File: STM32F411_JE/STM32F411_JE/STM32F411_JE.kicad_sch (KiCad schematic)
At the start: 1 part, among them U1 STM32F411CEU6

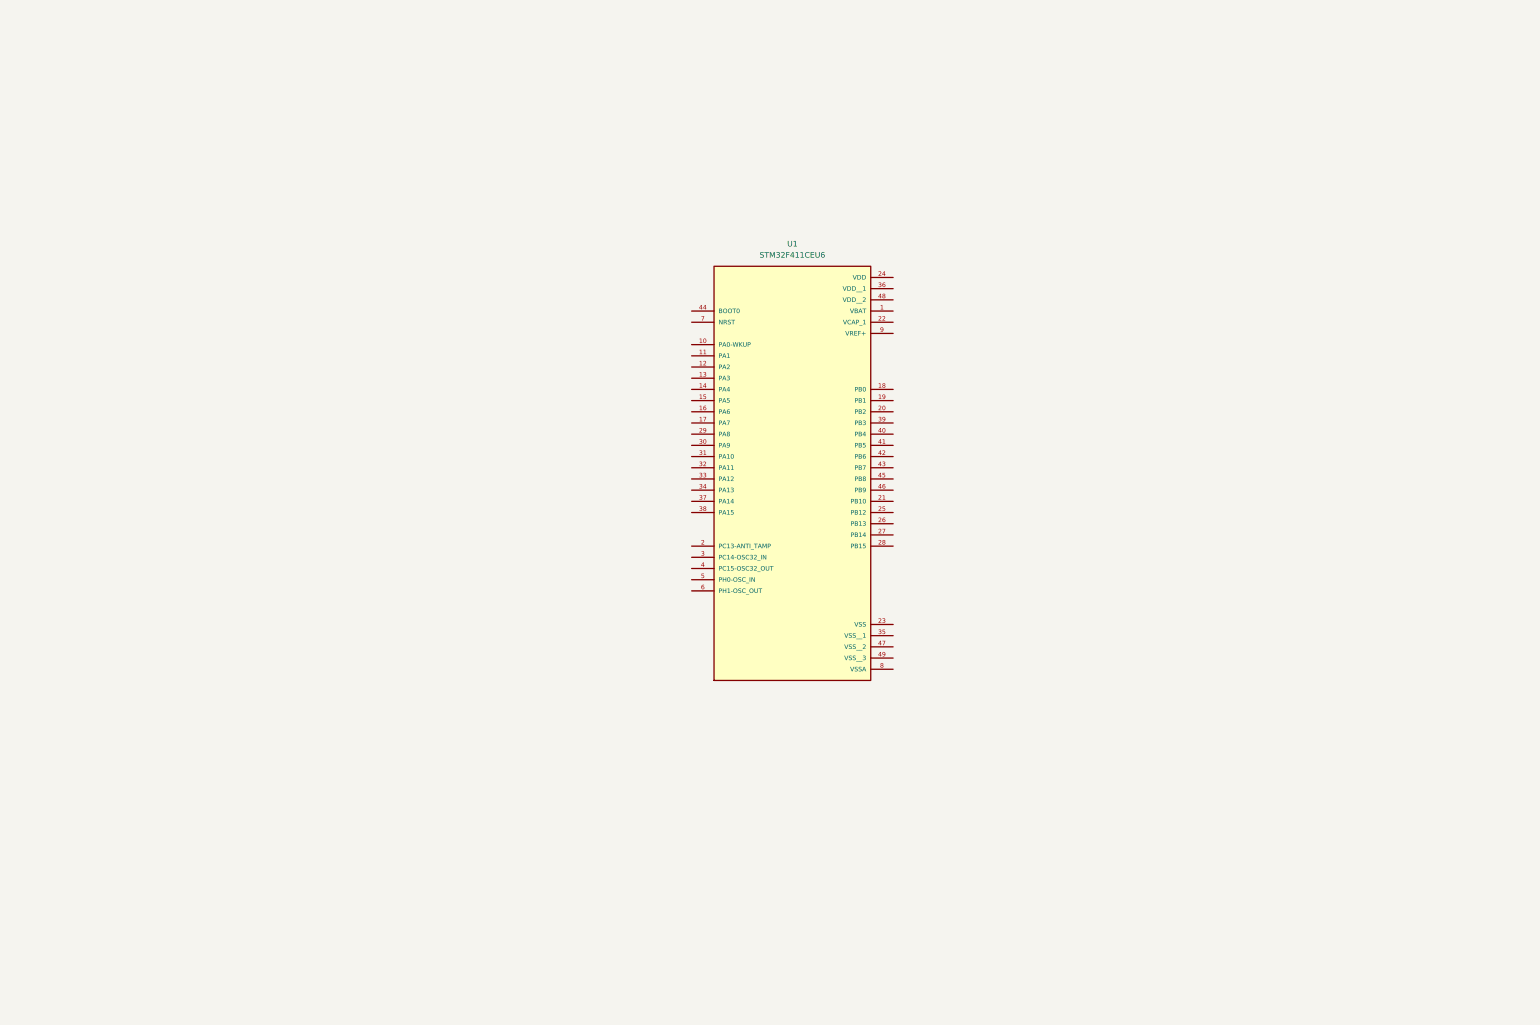
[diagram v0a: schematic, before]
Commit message: Se agrega el circuito de boot, de alimentación, de reset, y alimentación del rtc
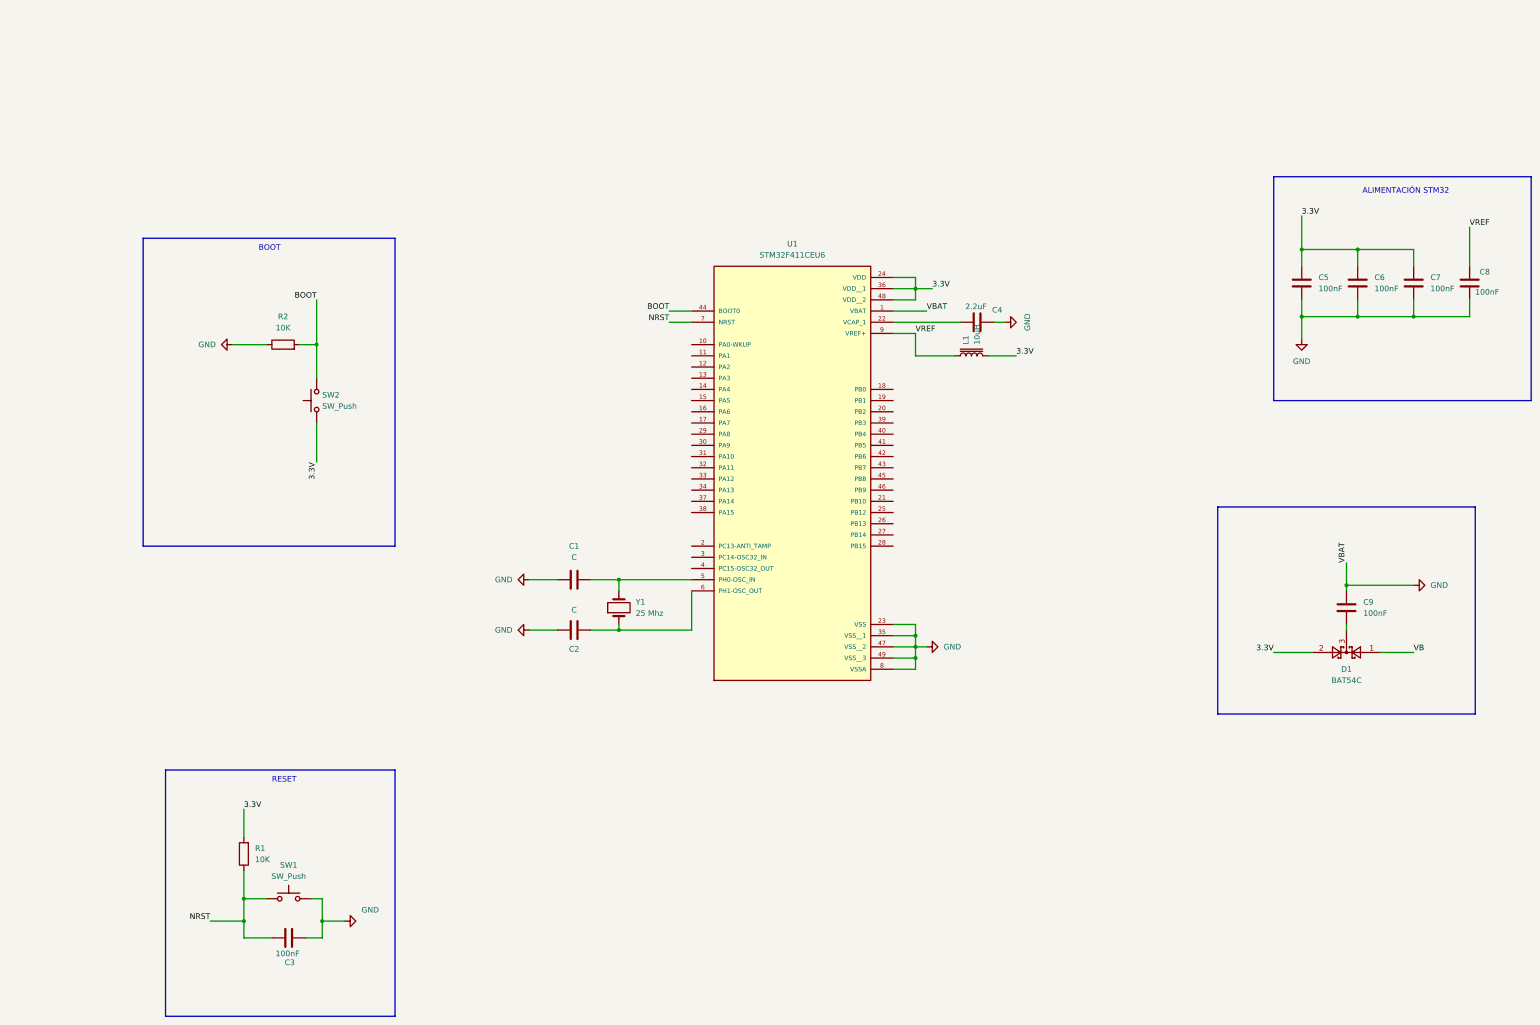
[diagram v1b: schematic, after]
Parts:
- added C1, C2: C, symbol Device:C
- added C3, C5, C6, C7, C8, C9: 100nF, Capacitor_SMD:C_0603_1608Metric_Pad1.08x0.95mm_HandSolder, symbol Device:C
- added C4: 2.2uF, Capacitor_SMD:C_0603_1608Metric_Pad1.08x0.95mm_HandSolder, symbol Device:C
- added D1: BAT54C, Package_TO_SOT_SMD:SOT-23, symbol Diode:BAT54C
- added L1: 10uH, Inductor_SMD:L_0603_1608Metric, symbol Device:L_Iron
- added R1, R2: 10K, Resistor_SMD:R_0603_1608Metric_Pad0.98x0.95mm_HandSolder, symbol Device:R
- added SW1, SW2: SW_Push, Button_Switch_SMD:SW_SPST_CK_RS282G05A3, symbol Switch:SW_Push
- added Y1: 25 Mhz, symbol Device:Crystal
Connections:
- net GND: now reaches U1.1 (VBAT)
- net GND: now also U1.23 (VSS), U1.35 (VSS__1), U1.47 (VSS__2), U1.49 (VSS__3), U1.8 (VSSA), C1.1, C2.1, C3.2, C4.1, C5.2, C6.2, C7.2, C8.2, C9.1, R2.1, SW1.2
- net at U1.22 (VCAP_1): now also C4.2
- net 3.3V: now reaches U1.24 (VDD)
- net 3.3V: now also U1.36 (VDD__1), U1.48 (VDD__2), C5.1, C6.1, C7.1, D1.2, L1.2, R1.2, SW2.1
- net BOOT: now reaches U1.44 (BOOT0)
- net BOOT: now also R2.2, SW2.2
- net at U1.5 (PH0-OSC_IN): now also C1.2, Y1.2
- net at U1.6 (PH1-OSC_OUT): now also C2.2, Y1.1
- net NRST: now reaches U1.7 (NRST)
- net NRST: now also C3.1, R1.1, SW1.1
- net VREF: now reaches U1.9 (VREF+)
- net VREF: now also C8.1, L1.1
- new net: C9.2, D1.3
- new net VB: D1.1
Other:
- note added: "ALIMENTACIÓN STM32"
- note added: "BOOT"
- note added: "RESET"

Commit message: Se termina el diseño esquematico de el STM32F411_JE
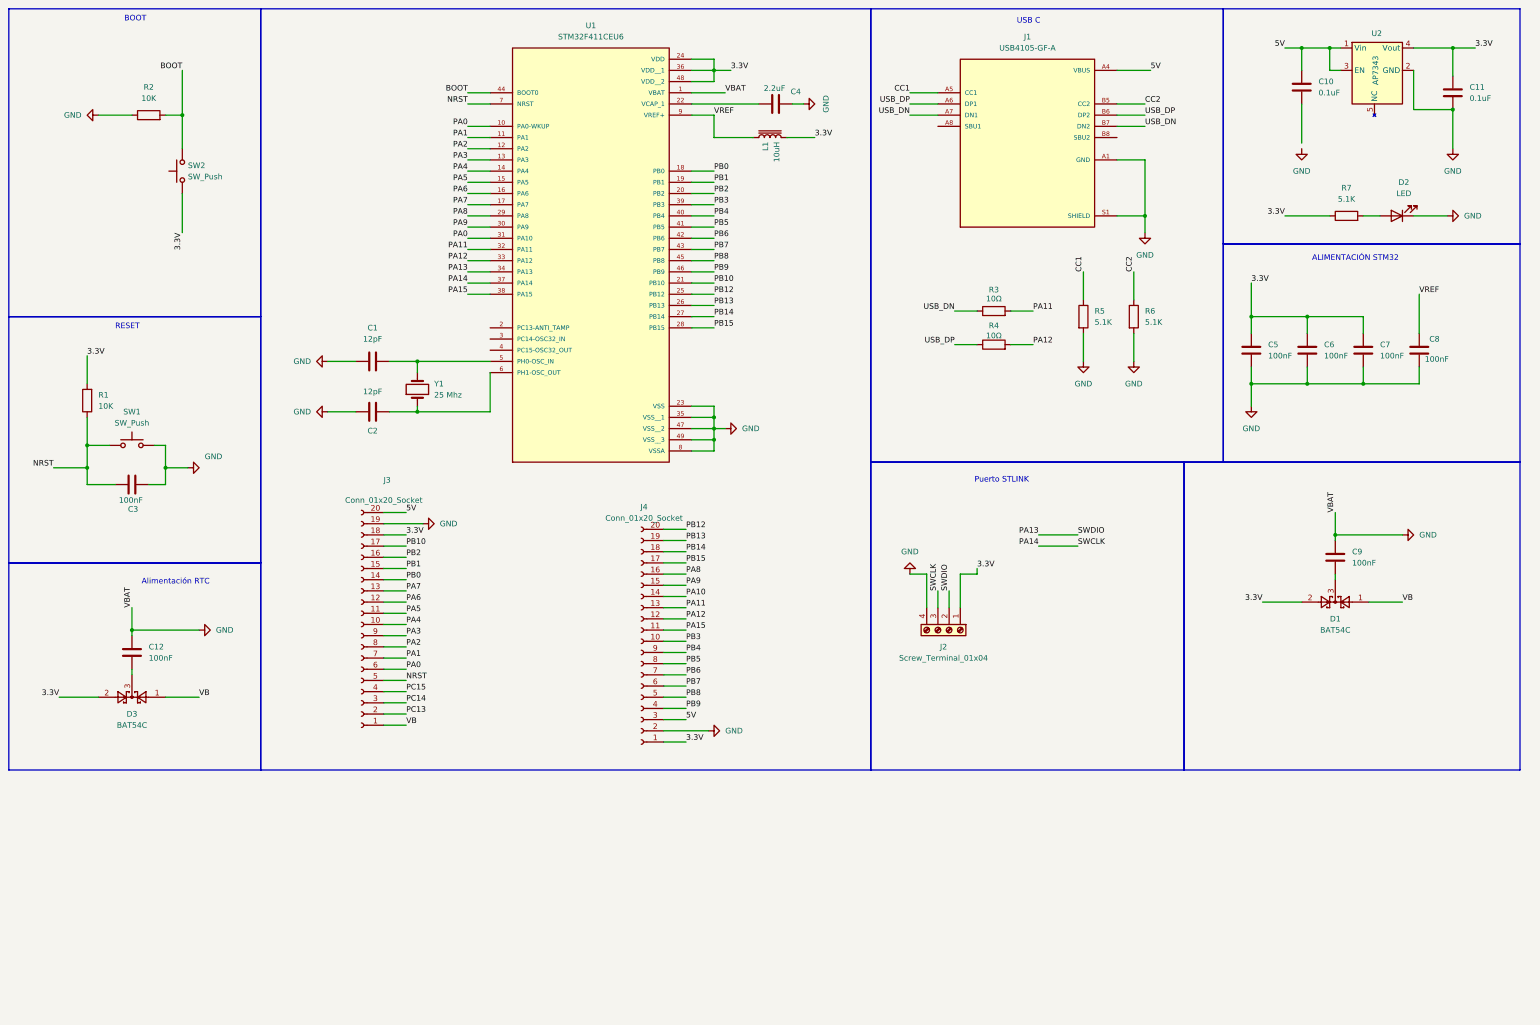
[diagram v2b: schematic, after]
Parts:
- added C10, C11: 0.1uF, Capacitor_SMD:C_0603_1608Metric_Pad1.08x0.95mm_HandSolder, symbol Device:C
- added C12: 100nF, Capacitor_SMD:C_0603_1608Metric_Pad1.08x0.95mm_HandSolder, symbol Device:C
- added D2: LED, LED_SMD:LED_0603_1608Metric, symbol Device:LED
- added D3: BAT54C, Package_TO_SOT_SMD:SOT-23, symbol Diode:BAT54C
- added J1: USB4105-GF-A, USB TYPE C:GCT_USB4105-GF-A, symbol USB_TYPE_C:USB4105-GF-A
- added J2: Screw_Terminal_01x04, Connector_PinHeader_2.54mm:PinHeader_1x04_P2.54mm_Horizontal, symbol Connector:Screw_Terminal_01x04
- added J3, J4: Conn_01x20_Socket, Connector_PinHeader_2.54mm:PinHeader_1x20_P2.54mm_Vertical, symbol Connector:Conn_01x20_Socket
- added R3, R4: 10Ω, Resistor_SMD:R_0603_1608Metric_Pad0.98x0.95mm_HandSolder, symbol Device:R
- added R5, R6: 5.1K, Resistor_SMD:R_0805_2012Metric, symbol Device:R
- added R7: 5.1K, Resistor_SMD:R_0603_1608Metric_Pad0.98x0.95mm_HandSolder, symbol Device:R
- added U2: AP7343, Package_TO_SOT_SMD:SOT-23-5, symbol ap7343:AP7343
- C1, C2: value C -> 12pF; footprint (none) -> Capacitor_SMD:C_0603_1608Metric_Pad1.08x0.95mm_HandSolder
- U1: footprint STM32F411CEU6:QFN50P700X700X60-49N -> STM32F411:QFN50P700X700X60-49N
- Y1: footprint (none) -> Crystal:Crystal_SMD_0603-2Pin_6.0x3.5mm
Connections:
- net 3.3V: now also C11.1, D3.2, J2.1 (Pin_1), J3.18 (Pin_18), J4.1 (Pin_1), R7.1, U2.4 (Vout)
- net GND: now also C11.2, C12.1, D2.1 (K), J1.A1 (GND), J1.S1 (SHIELD), J2.4 (Pin_4), J3.19 (Pin_19), J4.2 (Pin_2), R5.2, R6.2, U2.2 (GND)
- net NRST: now also J3.5 (Pin_5)
- net VB: now also D3.1, J3.1 (Pin_1)
- net PA0: now reaches U1.10 (PA0-WKUP)
- net PA0: now also U1.31 (PA10), J3.6 (Pin_6)
- net PA1: now reaches U1.11 (PA1)
- net PA1: now also J3.7 (Pin_7)
- net PA2: now reaches U1.12 (PA2)
- net PA2: now also J3.8 (Pin_8)
- net PA3: now reaches U1.13 (PA3)
- net PA3: now also J3.9 (Pin_9)
- net PA4: now reaches U1.14 (PA4)
- net PA4: now also J3.10 (Pin_10)
- net PA5: now reaches U1.15 (PA5)
- net PA5: now also J3.11 (Pin_11)
- net PA6: now reaches U1.16 (PA6)
- net PA6: now also J3.12 (Pin_12)
- net PA7: now reaches U1.17 (PA7)
- net PA7: now also J3.13 (Pin_13)
- net PB0: now reaches U1.18 (PB0)
- net PB0: now also J3.14 (Pin_14)
- net PB1: now reaches U1.19 (PB1)
- net PB1: now also J3.15 (Pin_15)
- net PB2: now reaches U1.20 (PB2)
- net PB2: now also J3.16 (Pin_16)
- net PB10: now reaches U1.21 (PB10)
- net PB10: now also J3.17 (Pin_17)
- net PB12: now reaches U1.25 (PB12)
- net PB12: now also J4.20 (Pin_20)
- net PB13: now reaches U1.26 (PB13)
- net PB13: now also J4.19 (Pin_19)
- net PB14: now reaches U1.27 (PB14)
- net PB14: now also J4.18 (Pin_18)
- net PB15: now reaches U1.28 (PB15)
- net PB15: now also J4.17 (Pin_17)
- net PA8: now reaches U1.29 (PA8)
- net PA8: now also J4.16 (Pin_16)
- net PA9: now reaches U1.30 (PA9)
- net PA9: now also J4.15 (Pin_15)
- net PA11: now reaches U1.32 (PA11)
- net PA11: now also J4.13 (Pin_13), R3.2
- net PA12: now reaches U1.33 (PA12)
- net PA12: now also J4.12 (Pin_12), R4.2
- net PA13: now reaches U1.34 (PA13)
- net PA13: now also J2.2 (Pin_2)
- net PA14: now reaches U1.37 (PA14)
- net PA14: now also J2.3 (Pin_3)
- net PA15: now reaches U1.38 (PA15)
- net PA15: now also J4.11 (Pin_11)
- net PB3: now reaches U1.39 (PB3)
- net PB3: now also J4.10 (Pin_10)
- net PB4: now reaches U1.40 (PB4)
- net PB4: now also J4.9 (Pin_9)
- net PB5: now reaches U1.41 (PB5)
- net PB5: now also J4.8 (Pin_8)
- net PB6: now reaches U1.42 (PB6)
- net PB6: now also J4.7 (Pin_7)
- net PB7: now reaches U1.43 (PB7)
- net PB7: now also J4.6 (Pin_6)
- net PB8: now reaches U1.45 (PB8)
- net PB8: now also J4.5 (Pin_5)
- net PB9: now reaches U1.46 (PB9)
- net PB9: now also J4.4 (Pin_4)
- new net: D2.2 (A), R7.2
- new net: C12.2, D3.3
- new net 5V: C10.1, J1.A4 (VBUS), J3.20 (Pin_20), J4.3 (Pin_3), U2.1 (Vin), U2.3 (EN)
- new net CC1: J1.A5 (CC1), R5.1
- new net CC2: J1.B5 (CC2), R6.1
- new net PA10: J4.14 (Pin_14)
- new net PC13: J3.2 (Pin_2)
- new net PC14: J3.3 (Pin_3)
- new net PC15: J3.4 (Pin_4)
- new net USB_DN: J1.A7 (DN1), J1.B7 (DN2), R3.1
- new net USB_DP: J1.A6 (DP1), J1.B6 (DP2), R4.1
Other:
- note added: "Alimentación RTC"
- note added: "Puerto STLINK"
- note added: "USB C"
- moved on the sheet: C1, C2, C3, C4, C5, C6, C7, C8, C9, D1, L1, R1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

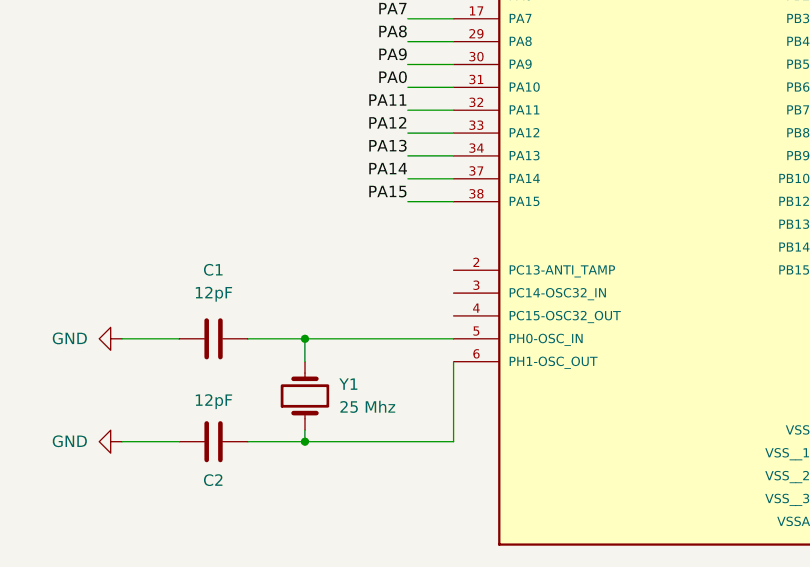
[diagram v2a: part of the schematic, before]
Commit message: Se agrega footprint a stm32
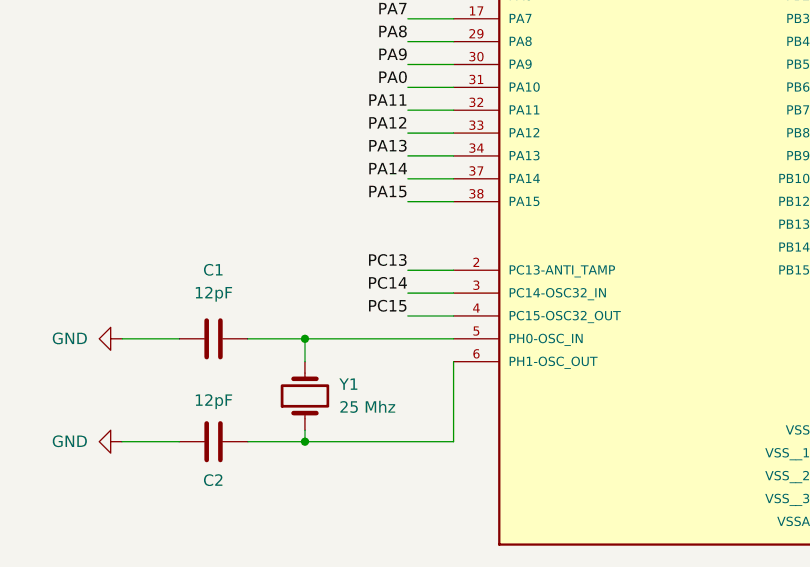
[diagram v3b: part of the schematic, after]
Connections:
- net PC13: now also U1.2 (PC13-ANTI_TAMP)
- net PC14: now also U1.3 (PC14-OSC32_IN)
- net PC15: now also U1.4 (PC15-OSC32_OUT)
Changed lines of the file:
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@@
+	(wire
+		(pts
+			(xy 130.81 101.6) (xy 135.89 101.6)
+		)
+		(stroke
+			(width 0)
+			(type default)
+		)
+	)
 	(wire
 		(pts
@@
 	(wire
 		(pts
+			(xy 130.81 106.68) (xy 135.89 106.68)
+		)
+		(stroke
+			(width 0)
+			(type default)
+		)
+	)
+	(wire
+		(pts
 			(xy 175.26 147.32) (xy 180.34 147.32)
 		)
@@
 		(pts
 			(xy 44.45 128.27) (xy 49.53 128.27)
+		)
+		(stroke
+			(width 0)
+			(type default)
+		)
+	)
+	(wire
+		(pts
+			(xy 130.81 104.14) (xy 135.89 104.14)
 		)
 		(stroke
@@
 		)
 	)
+	(label "PC15"
+		(at 130.81 106.68 180)
+		(fields_autoplaced yes)
+		(effects
+			(font
+				(size 1.27 1.27)
+			)
+			(justify right bottom)
+		)
+	)
 	(label "3.3V"
 		(at 38.1 185.42 180)
@@
 		)
 	)
+	(label "PC14"
+		(at 130.81 104.14 180)
+		(fields_autoplaced yes)
+		(effects
+			(font
+				(size 1.27 1.27)
+			)
+			(justify right bottom)
+		)
+	)
 	(label "SWDIO"
 		(at 269.24 148.59 0)
@@
 		)
 	)
+	(label "PC13"
+		(at 130.81 101.6 180)
+		(fields_autoplaced yes)
+		(effects
+			(font
+				(size 1.27 1.27)
+			)
+			(justify right bottom)
+		)
+	)
